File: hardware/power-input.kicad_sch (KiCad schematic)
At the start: 24 parts, among them J1 Micro-Fit 1x2, P1 #6 Fork Spade, P1 NEMA5-15P Cord, P2 #6 Fork Spade, P3 #6 Fork Spade, P4 #6 Fork Spade, P5 #6 Fork Spade, P6 Micro-Fit 3.0 1x2, P7 Banana 1x2, P8 Micro-Fit 3.0 1x2

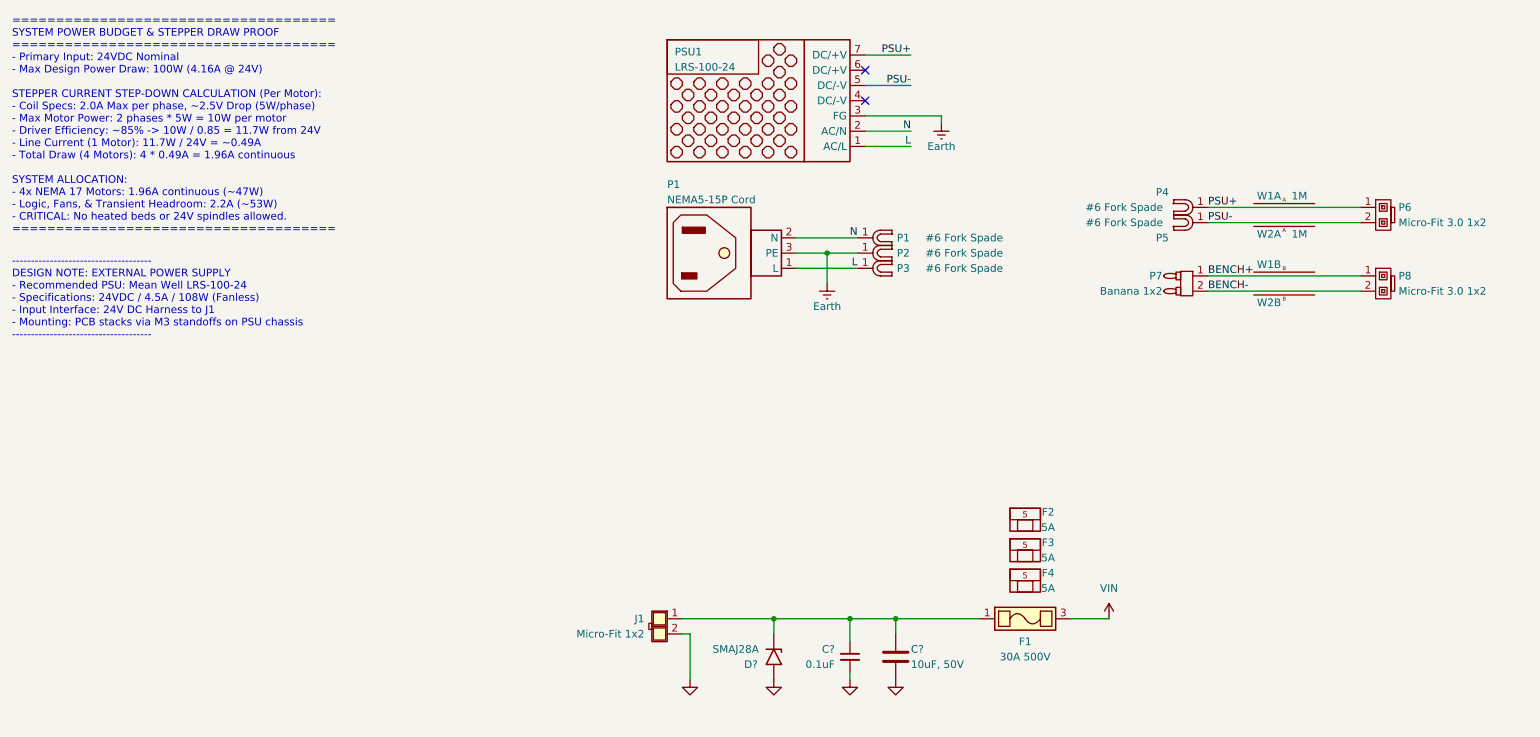
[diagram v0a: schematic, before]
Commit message: Finish power input
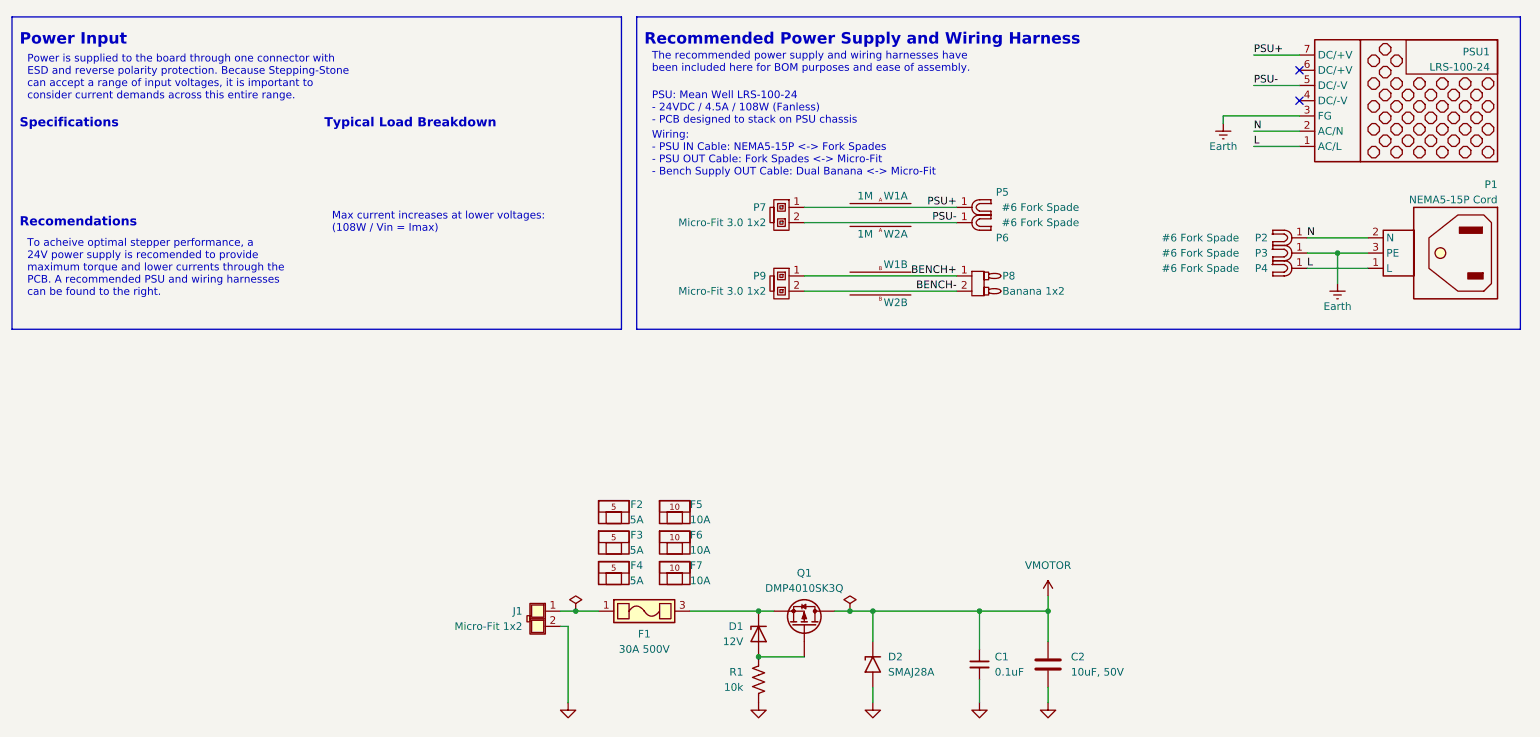
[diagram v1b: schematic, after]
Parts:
- removed P6, P8: Micro-Fit 3.0 1x2, symbol stepping-stone:Micro-Fit_3.0_1x2 Plug
- added D1: 12V, Package_TO_SOT_SMD:SOT-23, symbol Diode:BZX84Cxx
- added F5, F6, F7: 10A, symbol stepping-stone:0891010.NXS
- added P7, P9: Micro-Fit 3.0 1x2, symbol stepping-stone:Micro-Fit 3.0 1x2 Plug
- added Q1: DMP4010SK3Q, Package_TO_SOT_SMD:TO-252-2, symbol stepping-stone:DMP4010SK3Q-13
- added R1: 10k, Resistor_SMD:R_0603_1608Metric, symbol Device:R_US
- gave numbers to parts that had none: 3
- renumbered P1 to P2, P2 to P3, P3 to P4, P4 to P5, P5 to P6, P7 to P8, W1 to W3, W2 to W4, W3 to W5, W4 to W6
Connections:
- net BENCH+: now also P9.1
- net BENCH-: now also P9.2
- net GND: now also R1.2
- net PSU+: now also P7.1
- net PSU-: now also P7.2
- net at F1.1, F1.2, J1.1: no longer C1.1, C2.1, D2.1 (A1)
- net VIN: no longer names the net of F1.3, F1.4
- net VIN: now also D1.3 (K), Q1.3 (S)
- new net: D1.1 (A), Q1.1 (G), R1.1
- new net VMOTOR: C1.1, C2.1, D2.1 (A1), Q1.2 (D)
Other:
- note added: "Max current increases at lower voltages: (108W / Vin = Imax)"
- note added: "PSU: Mean Well LRS-100-24 - 24VDC / 4.5A / 108W (Fanless) - PCB designed to stack on PSU chassis"
- note added: "Power Input"
- note added: "Power is supplied to the board through one connector with ESD and reverse polarity protection. Because Stepping-Stone can accept a range of input voltages, it is important to consider current demands across this entire range."
- note added: "Recomendations"
- note added: "Recommended Power Supply and Wiring Harness"
- note added: "Specifications"
- note added: "The recommended power supply and wiring harnesses have been included here for BOM purposes and ease of assembly."
- note added: "To acheive optimal stepper performance, a 24V power supply is recomended to provide maximum torque and lower currents through the PCB. A recommended PSU and wiring harnesses can be found to the right."
- note added: "Typical Load Breakdown"
- note added: "Wiring: - PSU IN Cable: NEMA5-15P <-> Fork Spades - PSU OUT Cable: Fork Spades <-> Micro-Fit - Bench Supply OUT Cable: Dual Banana <-> Micro-Fit"
- note removed: "------------------------------------- DESIGN NOTE: EXTERNAL POWER SUPPLY - Recommended PSU: Mean Well LRS-100-24 - Specifications: 24VDC / 4.5A / 108W (Fanless) - Input Interface: 24V DC Harness to J1 - Mounting: PCB stacks via M3 standoffs on PSU chassis -------------------------------------"
- note removed: "===================================== SYSTEM POWER BUDGET & STEPPER DRAW PROOF ===================================== - Primary Input: 24VDC Nominal - Max Design Power Draw: 100W (4.16A @ 24V) STEPPER CURRENT STEP-DOWN CALCULATION (Per Motor): - Coil Specs: 2.0A Max per phase, ~2.5V Drop (5W/phase) - Max Motor Power: 2 phases * 5W = 10W per motor - Driver Efficiency: ~85% -> 10W / 0.85 = 11.7W fro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"
- moved on the sheet: C1, C2, D2, F1, F2, F3, F4, J1, P1, P2, P3, P4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

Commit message: Update power input connector and buck converter
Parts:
- removed J1: Micro-Fit 1x2, symbol stepping-stone:Micro-Fit 3.0 1x2 Jack
- removed P7, P9: Micro-Fit 3.0 1x2, symbol stepping-stone:Micro-Fit 3.0 1x2 Plug
- removed W3, W4, W5, W6: 18 AWG Crimp, symbol stepping-stone:Micro-Fit 3.0 18AWG Crimp
- added J1: XT30PW-M, symbol stepping-stone:XT30PW-M
- added P7, P9: XT30U-F, symbol stepping-stone:XT30U-F
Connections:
- net BENCH+: now also P9.+
- net BENCH-: now also P9.-
- net GND: now also J1.-
- net PSU+: now also P7.+
- net PSU-: now also P7.-
- net at F1.1, F1.2: now also J1.+
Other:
- note added: "Wiring: - PSU IN Cable: NEMA5-15P <-> Fork Spades - PSU OUT Cable: Fork Spades <-> XT30 - Bench Supply OUT Cable: Dual Banana <-> XT30"
- note removed: "Wiring: - PSU IN Cable: NEMA5-15P <-> Fork Spades - PSU OUT Cable: Fork Spades <-> Micro-Fit - Bench Supply OUT Cable: Dual Banana <-> Micro-Fit"

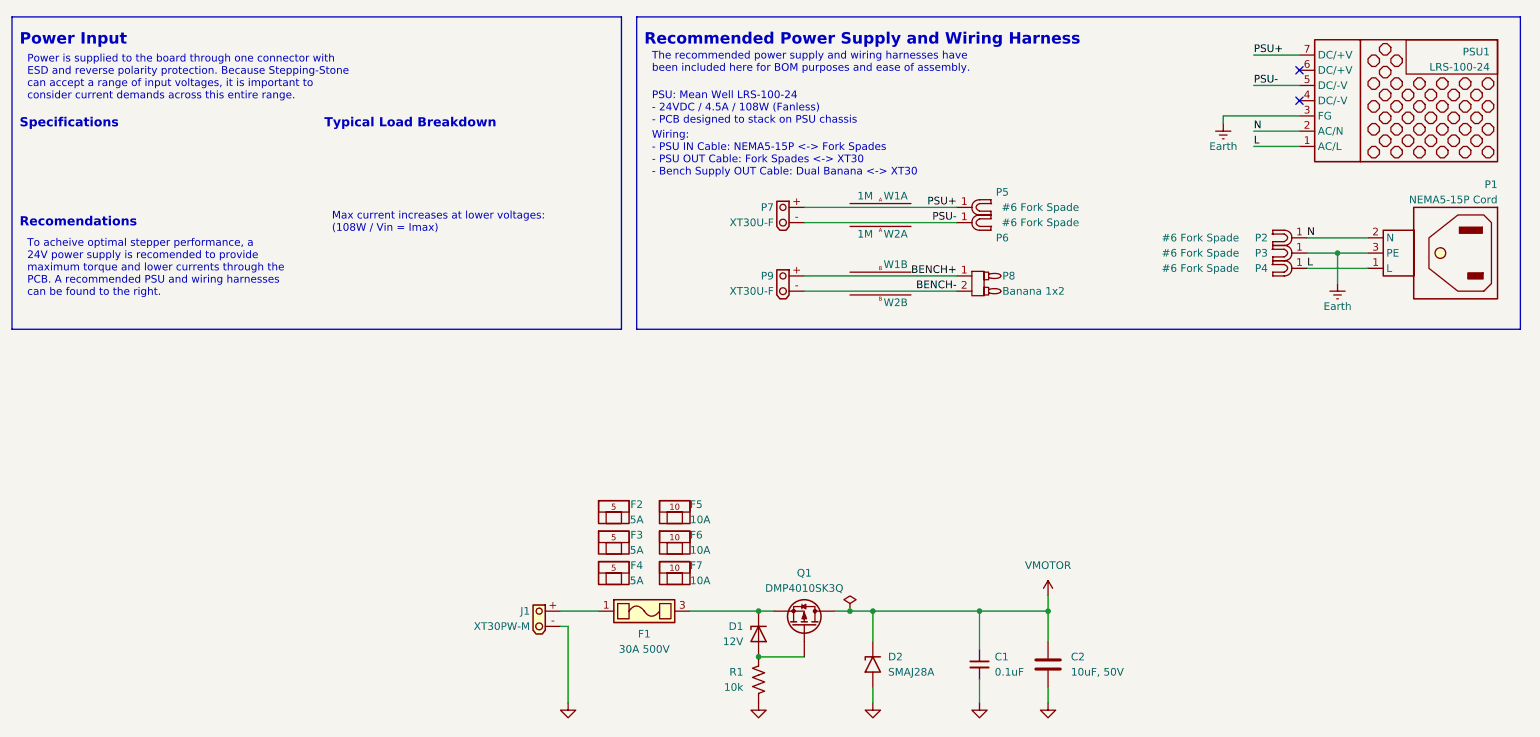
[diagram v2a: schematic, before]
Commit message: Added USB and began estop
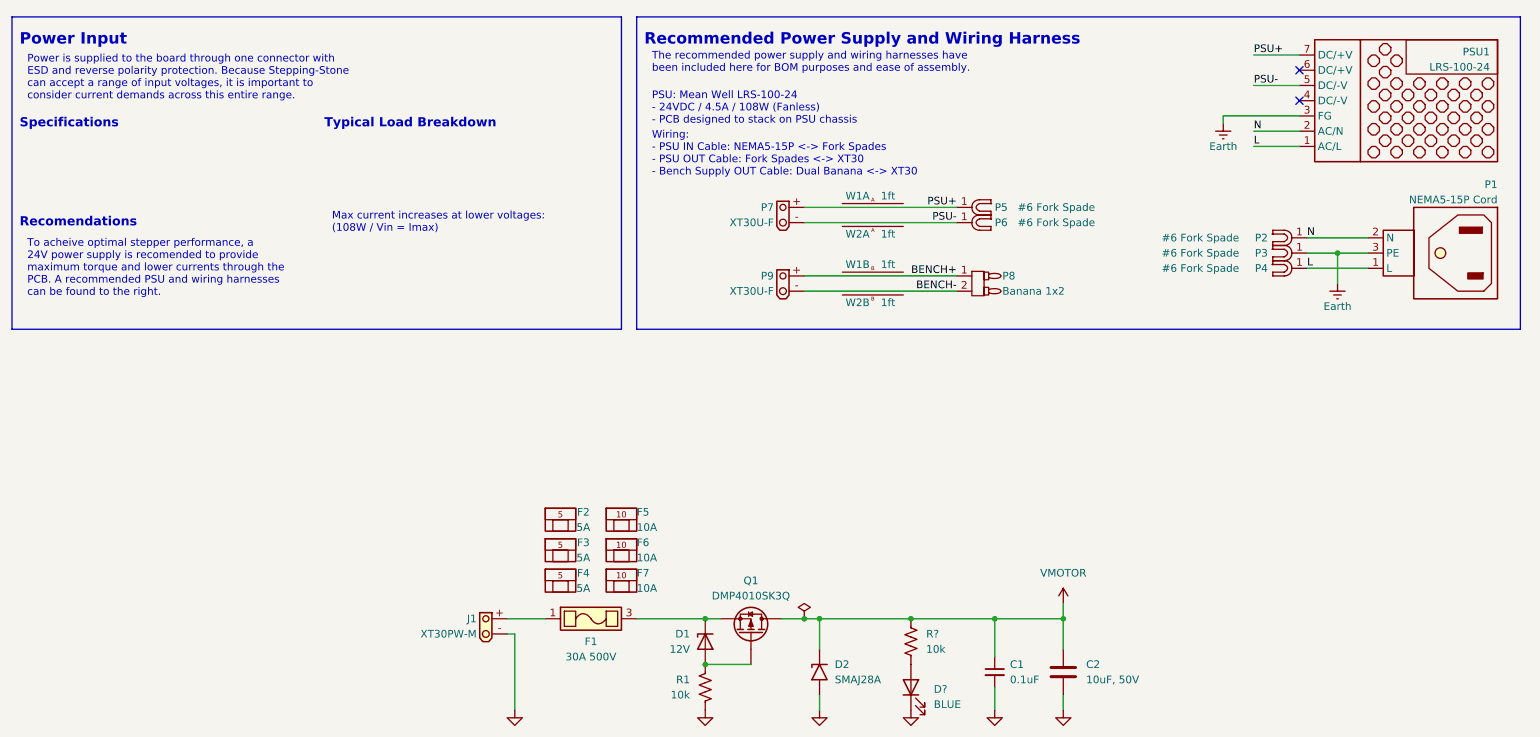
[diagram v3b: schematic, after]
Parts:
- removed P2, P3, P4, P5, P6: #6 Fork Spade, symbol stepping-stone:#6 Fork Spade
- removed W1: 1M, symbol stepping-stone:18AWG Stranded Red Wire
- removed W2: 1M, symbol stepping-stone:18AWG Stranded Black Wire
- added D?: BLUE, Diode_SMD:D_0805_2012Metric, symbol Device:LED
- added P2, P3, P4: #6 Fork Spade, symbol stepping-stone:18-22AWG #6 Fork Spade
- added P5, P6: #6 Fork Spade, symbol stepping-stone:14-16AWG #6 Fork Spade
- added R?: 10k, Resistor_SMD:R_0603_1608Metric, symbol Device:R_US
- added W1: 1ft, symbol stepping-stone:16AWG Stranded Red Wire
- added W2: 1ft, symbol stepping-stone:16AWG Stranded Black Wire
- J1: Vendor URL amazon.com/Amass-XT30PW-Upgrade-Connectors-Battery/dp/B099F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 -> https://octopart.com/part/amass/XT30PW-M
- P8: Vendor URL (none) -> https://www.digikey.com/en/products/detail/pomona-electroni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
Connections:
- net Earth: now also P3.1
- net GND: now also D?.1 (K)
- net L: now also P4.1
- net N: now also P2.1
- net PSU+: now also P5.1
- net PSU-: now also P6.1
- net VMOTOR: now also R?.1
- new net: D?.2 (A), R?.2
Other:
- moved on the sheet: C1, C2, D1, D2, F1, F2, F3, F4, F5, F6, F7, J1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

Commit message: Update LEDs
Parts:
- D?: value BLUE -> YELLOW; Part Number LTST-C171TBKT -> LTST-C170YKT; Vendor URL https://www.digikey.com/en/products/detail/liteon/LTST-C171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 -> https://www.digikey.com/en/products/detail/liteon/LTST-C170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
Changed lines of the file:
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@@
 			)
 		)
-		(property "Value" "BLUE"
+		(property "Value" "YELLOW"
 			(at 167.64 128.5874 90)
 			(show_name no)
@@
 			)
 		)
-		(property "Part Number" "LTST-C171TBKT"
+		(property "Part Number" "LTST-C170YKT"
 			(at 163.83 125.73 0)
 			(hide yes)
@@
 			)
 		)
-		(property "Vendor URL" "https://www.digikey.com/en/products/detail/liteon/LTST-C171TBKT/388528"
+		(property "Vendor URL" "https://www.digikey.com/en/products/detail/liteon/LTST-C170YKT/269222"
 			(at 163.83 125.73 0)
 			(hide yes)

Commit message: Add QSPI Flash
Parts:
- gave numbers to parts that had none: 2
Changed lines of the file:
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@@
 	)
 	(junction
+		(at 156.21 114.3)
+		(diameter 0)
+		(color 0 0 0 0)
+	)
+	(junction
 		(at 177.8 114.3)
 		(diameter 0)
@@
 	)
 	(junction
-		(at 146.05 114.3)
-		(diameter 0)
-		(color 0 0 0 0)
-	)
-	(junction
 		(at 148.59 114.3)
 		(diameter 0)
@@
 	(wire
 		(pts
-			(xy 148.59 114.3) (xy 163.83 114.3)
+			(xy 148.59 114.3) (xy 156.21 114.3)
 		)
 		(stroke
@@
 	(wire
 		(pts
-			(xy 146.05 114.3) (xy 148.59 114.3)
+			(xy 142.24 114.3) (xy 148.59 114.3)
 		)
 		(stroke
@@
 	(wire
 		(pts
-			(xy 142.24 114.3) (xy 146.05 114.3)
-		)
-		(stroke
-			(width 0)
-			(type default)
-		)
-	)
-	(wire
-		(pts
 			(xy 189.23 111.76) (xy 189.23 114.3)
 		)
@@
 	(wire
 		(pts
+			(xy 156.21 114.3) (xy 163.83 114.3)
+		)
+		(stroke
+			(width 0)
+			(type default)
+		)
+	)
+	(wire
+		(pts
 			(xy 228.6 35.56) (xy 220.98 35.56)
 		)
@@
 	)
 	(symbol
+		(lib_id "power:PWR_FLAG")
+		(at 156.21 114.3 0)
+		(unit 1)
+		(body_style 1)
+		(exclude_from_sim no)
+		(in_bom yes)
+		(on_board yes)
+		(in_pos_files yes)
+		(dnp no)
+		(fields_autoplaced yes)
+		(property "Reference" "#FLG01"
+			(at 156.21 112.395 0)
+			(hide yes)
+			(show_name no)
+			(do_not_autoplace no)
+			(effects
+				(font
+					(size 1.27 1.27)
+				)
+			)
+		)
+		(property "Value" "PWR_FLAG"
+			(at 156.21 109.22 0)
+			(hide yes)
+			(show_name no)
+			(do_not_autoplace no)
+			(effects
+				(font
+					(size 1.27 1.27)
+				)
+			)
+		)
+		(property "Footprint" ""
+			(at 156.21 114.3 0)
+			(hide yes)
+			(show_name no)
+			(do_not_autoplace no)
+			(effects
+				(font
+					(size 1.27 1.27)
+				)
+			)
+		)
+		(property "Datasheet" ""
+			(at 156.21 114.3 0)
+			(hide yes)
+			(show_name no)
+			(do_not_autoplace no)
+			(effects
+				(font
+					(size 1.27 1.27)
+				)
+			)
+		)
+		(property "Description" "Special symbol for telling ERC where power comes from"
+			(at 156.21 114.3 0)
+			(hide yes)
+			(show_name no)
+			(do_not_autoplace no)
+			(effects
+				(font
+					(size 1.27 1.27)
+				)
+			)
+		)
+		(pin "1"
+		)
+		(instances
+			(project "stepping-stone"
+				(path "/793a882e-3f7b-468b-a863-41a1f527e1bf/73c4e66b-e11c-48b6-b2c8-fbbf612d64c5"
+					(reference "#FLG01")
+					(unit 1)
+				)
+			)
+		)
+	)
+	(symbol
 		(lib_id "power:GND")
 		(at 163.83 129.54 0)
@@
 		(in_pos_files yes)
 		(dnp no)
-		(property "Reference" "R?"
+		(property "Reference" "R10"
 			(at 166.37 116.8399 0)
 			(show_name no)
@@
 			(project "stepping-stone"
 				(path "/793a882e-3f7b-468b-a863-41a1f527e1bf/73c4e66b-e11c-48b6-b2c8-fbbf612d64c5"
-					(reference "R?")
-					(unit 1)
-				)
-			)
-		)
-	)
-	(symbol
-		(lib_id "power:PWR_FLAG")
-		(at 146.05 114.3 0)
-		(unit 1)
-		(body_style 1)
-		(exclude_from_sim no)
-		(in_bom yes)
-		(on_board yes)
-		(in_pos_files yes)
-		(dnp no)
-		(fields_autoplaced yes)
-		(property "Reference" "#FLG02"
-			(at 146.05 112.395 0)
-			(hide yes)
-			(show_name no)
-			(do_not_autoplace no)
-			(effects
-				(font
-					(size 1.27 1.27)
-				)
-			)
-		)
-		(property "Value" "PWR_FLAG"
-			(at 146.05 109.22 0)
-			(hide yes)
-			(show_name no)
-			(do_not_autoplace no)
-			(effects
-				(font
-					(size 1.27 1.27)
-				)
-			)
-		)
-		(property "Footprint" ""
-			(at 146.05 114.3 0)
-			(hide yes)
-			(show_name no)
-			(do_not_autoplace no)
-			(effects
-				(font
-					(size 1.27 1.27)
-				)
-			)
-		)
-		(property "Datasheet" ""
-			(at 146.05 114.3 0)
-			(hide yes)
-			(show_name no)
-			(do_not_autoplace no)
-			(effects
-				(font
-					(size 1.27 1.27)
-				)
-			)
-		)
-		(property "Description" "Special symbol for telling ERC where power comes from"
-			(at 146.05 114.3 0)
-			(hide yes)
-			(show_name no)
-			(do_not_autoplace no)
-			(effects
-				(font
-					(size 1.27 1.27)
-				)
-			)
-		)
-		(pin "1"
-		)
-		(instances
-			(project "stepping-stone"
-				(path "/793a882e-3f7b-468b-a863-41a1f527e1bf/73c4e66b-e11c-48b6-b2c8-fbbf612d64c5"
-					(reference "#FLG02")
+					(reference "R10")
 					(unit 1)
 				)
@@
 		(dnp no)
 		(fields_autoplaced yes)
-		(property "Reference" "D?"
+		(property "Reference" "D4"
 			(at 167.64 126.0474 90)
 			(show_name no)
@@
 			(project "stepping-stone"
 				(path "/793a882e-3f7b-468b-a863-41a1f527e1bf/73c4e66b-e11c-48b6-b2c8-fbbf612d64c5"
-					(reference "D?")
+					(reference "D4")
 					(unit 1)
 				)

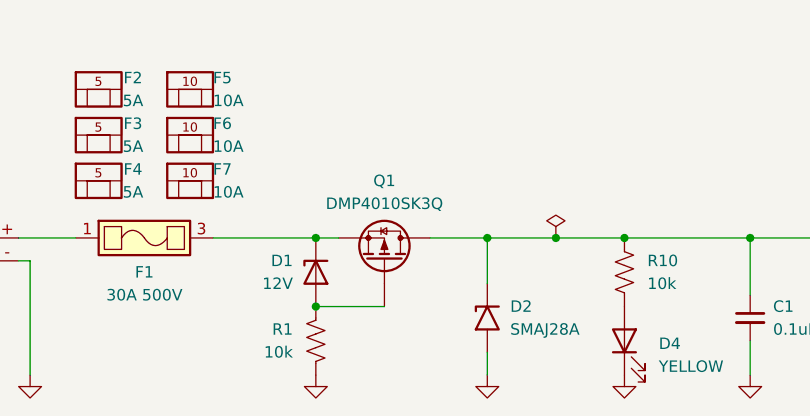
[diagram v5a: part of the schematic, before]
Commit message: Adjust power input protection
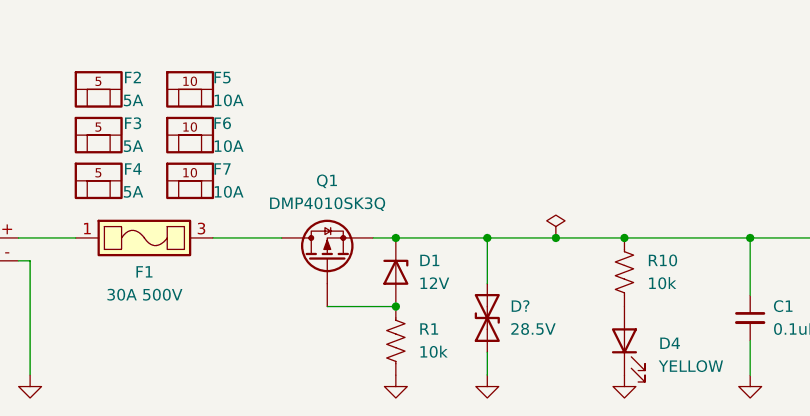
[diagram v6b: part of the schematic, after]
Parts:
- removed D2: SMAJ28A, Diode_SMD:D_SMA, symbol Diode:SMAJ28A
- added D?: 28.5V, Diode_SMD:D_SMB, symbol Device:D_TVS
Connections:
- net GND: now also D?.1 (A1)
- net VMOTOR: now also D1.3 (K), Q1.3 (S), D?.2 (A2); no longer Q1.2 (D)
- net at F1.3, F1.4: now also Q1.2 (D); no longer D1.3 (K), Q1.3 (S)
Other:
- moved on the sheet: D1, Q1, R1
